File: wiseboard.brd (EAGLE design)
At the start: 100 x 80 mm, 87 parts, among them CN1 455-1749-1-ND, CN3 455-1749-1-ND, IC1 MCP73871-2CCI/ML-ND, IC2 LM358MX, Q1 IRLML6402TRPBF, Q2 IRLML6402TRPBF, U1 LT1945EMSPBF, X1 1528-1438-ND

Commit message: move all components onto test area and also test commit
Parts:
- moved R35 846.5 mm to (30.5, 38.1)
- moved R34 840.7 mm to (38.1, 38.1)
- moved R33 833.5 mm to (44.5, 36.8)
- moved S7 812.3 mm to (30.5, 34.3)
- moved S6 789.6 mm to (34.3, 30.5)
- moved S5 788.8 mm to (30.5, 50.8)
- moved S3 750.5 mm to (55.9, 45.7)
- moved S4 750.0 mm to (39.4, 29.2)
- moved C13 706.8 mm to (68.6, 7.62)
- moved C16 703.3 mm to (83.8, 78.7)
- moved JP3 703.3 mm to (78.7, 78.7)
- moved R20 703.3 mm to (80.0, 72.4)
- moved R29 703.3 mm to (80.0, 35.6)
- moved R30 703.3 mm to (80.0, 27.9)
- moved R31 703.3 mm to (80.0, 20.3)
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
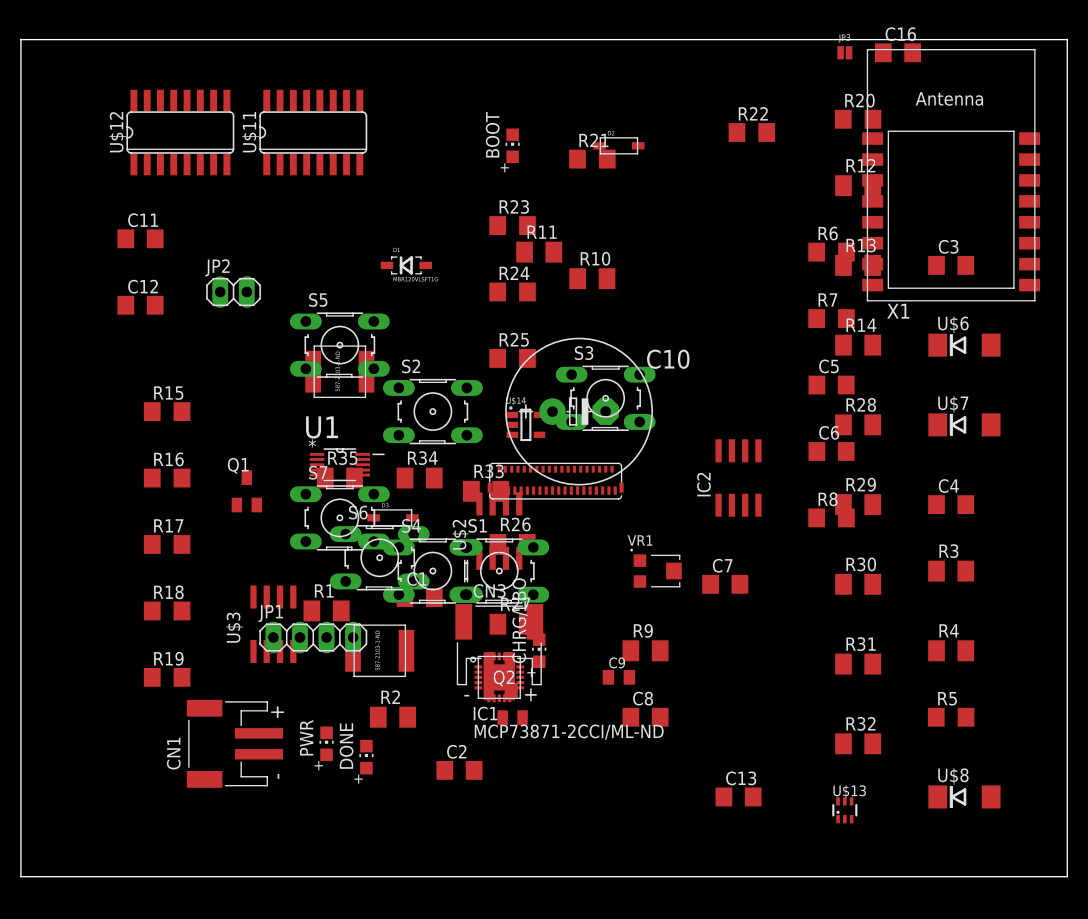
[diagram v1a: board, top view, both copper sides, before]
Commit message: ADD ESP DEBUG HEADERS AND ROUGH AUTOROUTE
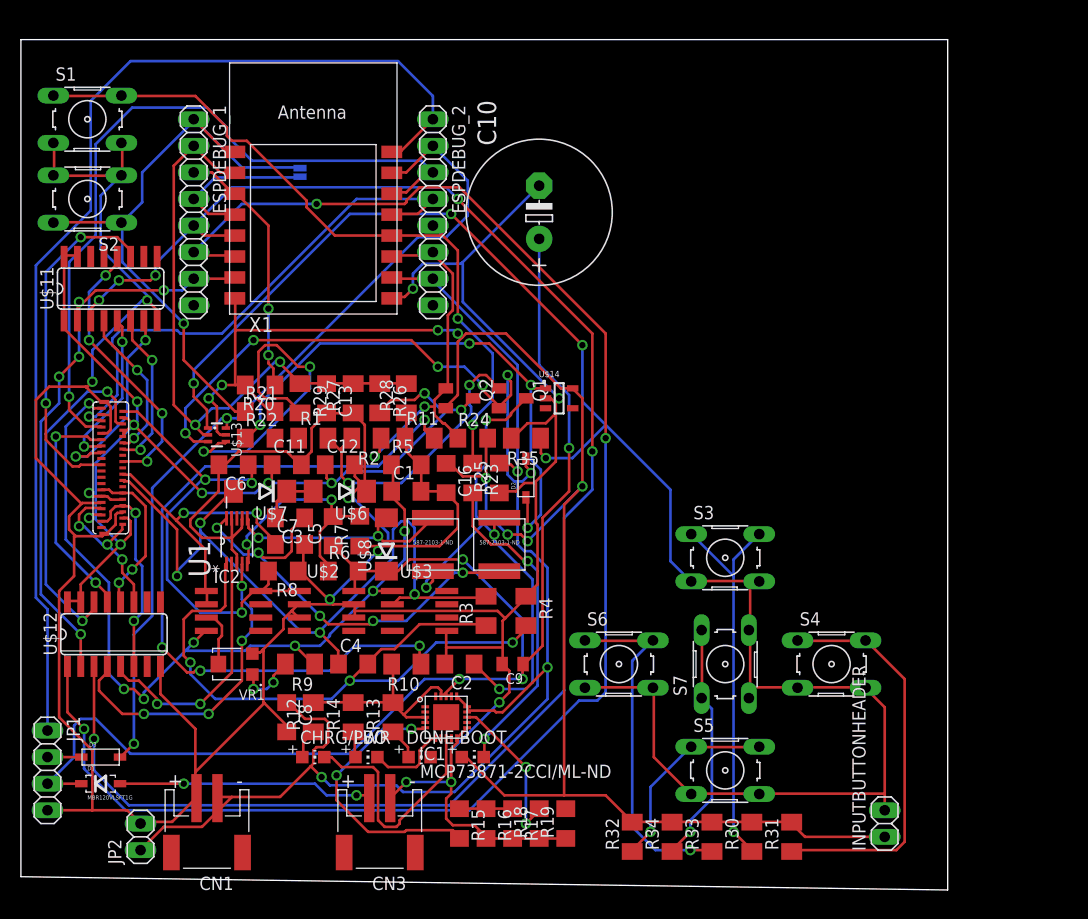
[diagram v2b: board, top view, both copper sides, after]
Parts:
- added ESPDEBUG_1, ESPDEBUG_2: (no value), pinhead:1X08
- added INPUTBUTTONHEADER: (no value), pinhead:1X02
- moved R12 72.7 mm to (27.9, 15.2), turned to 90 degrees
- moved U$13 69.9 mm to (18.7, 42.2), turned to 270 degrees
- moved C3 67.6 mm to (25.7, 34.3), turned to 180 degrees
- moved U$7 67.6 mm to (22.9, 36.8), turned to 180 degrees
- moved R20 62.5 mm to (22.9, 47.0), turned to 180 degrees
- moved R13 62.0 mm to (35.6, 15.2), turned to 90 degrees
- moved U$6 61.3 mm to (30.5, 36.8), turned to 180 degrees
- moved X1 61.0 mm to (27.9, 64.8)
- moved U$8 60.3 mm to (34.9, 31.8), turned to 90 degrees
- moved R14 59.9 mm to (31.8, 15.2), turned to 90 degrees
- moved C16 59.3 mm to (40.6, 38.1), turned to 270 degrees
- moved C4 59.1 mm to (31.8, 20.3)
- moved BOOT 58.5 mm to (43.2, 11.4), turned to 270 degrees
- moved S1 58.4 mm to (6.35, 72.4)
- moved D1 57.5 mm to (7.62, 8.89)
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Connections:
- removed net GPIO2: R24.1
- removed net N$12: JP3.1, X1.4
- removed net N$17: C8.1, CN1.2, IC1.14, IC1.15, IC1.16, JP2.1
- new net +3V1: ESPDEBUG_1.8
- new net GND1: ESPDEBUG_2.8
- new net GPIO16: ESPDEBUG_1.4, JP3.1, X1.4
- net +3V3: now also INPUTBUTTONHEADER.1
- net ADC: now also ESPDEBUG_1.2
- net BOOSTENA: now also ESPDEBUG_2.6, R24.1
- net CH_PD: now also ESPDEBUG_1.3
- net CL: now also ESPDEBUG_2.4
- net GPIO0: now also ESPDEBUG_2.5
- net GPIO12: now also ESPDEBUG_1.6; no longer U$13.6
- net GPIO13: now also ESPDEBUG_1.7
- net GPIO14: now also ESPDEBUG_1.5
- net GPIO15: now also ESPDEBUG_2.7
- net N$25: now also U$14.1
- net N$26: now also INPUTBUTTONHEADER.2
- net OE: now also ESPDEBUG_2.3
- net RESET: now also ESPDEBUG_1.1
- net RXD: now also ESPDEBUG_2.2, U$13.6
- net TXD: now also ESPDEBUG_2.1
- net VBAT: now also C8.1, CN1.2, IC1.14, IC1.15, IC1.16, JP2.1; no longer U$14.1
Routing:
- net GND: track 0.00 -> 404.0 mm, vias 0 -> 10
- net +3V3: track 0.00 -> 171.1 mm, vias 0 -> 8
- net N$26: track 0.00 -> 170.7 mm, vias 0 -> 4
- net GPIO14: track 0.00 -> 160.7 mm, vias 0 -> 6
- net VCC: track 0.00 -> 157.2 mm, vias 0 -> 4
- net GPIO12: track 0.00 -> 152.8 mm, vias 0 -> 3
- net VBAT: track 0.00 -> 150.4 mm, vias 0 -> 8
- net VDD: track 0.00 -> 106.8 mm, vias 0 -> 10
- net TXD: track 0.00 -> 105.9 mm
- net -15V: track 0.00 -> 82.1 mm, vias 0 -> 7
- net RXD: track 0.00 -> 82.0 mm, vias 0 -> 2
- net +20V: track 0.00 -> 72.7 mm, vias 0 -> 4
- net N$9: track 0.00 -> 72.5 mm, vias 0 -> 4
- net OE: track 0.00 -> 71.7 mm, vias 0 -> 1
- net GPIO0: track 0.00 -> 69.4 mm, vias 0 -> 2
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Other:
- board size 100 x 80 mm -> 88.6 x 81.3 mm

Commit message: PASS ERC SCHEMATIC TEST AND ADD SUPPLY SYMBOLS
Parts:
- removed C13: 1uF, adafruit:C1206
- added INPUTBUTTONHEADER1, SOLARPIN: (no value), pinhead:1X02
- C2: value (none) -> 2u2F
- C4: value (none) -> 100pF
- moved JP1 59.1 mm to (46.4, 49.8), turned to 180 degrees
- moved C10 53.1 mm to (26.7, 15.6), turned to 0 degrees
- moved IC2 52.9 mm to (-10.2, -17.8), turned to 0 degrees
- moved D3 52.7 mm to (47.6, 45.7), turned to 270 degrees
- moved ESPDEBUG_1 49.7 mm to (64.1, 49.2), turned to 180 degrees
- moved JP3 47.3 mm to (67.9, 44.1), turned to 0 degrees
- moved X1 46.5 mm to (66.7, 39.1), turned to 270 degrees
- moved BOOT 44.6 mm to (24.8, 52.1), turned to 180 degrees
- moved 22 44.0 mm to (3.81, 45.1)
- moved ESPDEBUG_2 43.1 mm to (64.1, 28.3), turned to 180 degrees
- moved C2 42.7 mm to (11.4, 50.2), turned to 0 degrees
- moved R4 42.5 mm to (14.6, 51.4), turned to 90 degrees
- moved R29 35.2 mm to (46.4, 16.5), turned to 0 degrees
- moved DONE 35.1 mm to (3.17, 7.62), turned to 90 degrees
- moved S2 34.6 mm to (37.5, 49.5), turned to 90 degrees
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- renumbered CN3 to SOLAR
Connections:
- net +20V renamed -20V
- removed net +24V: U$4.P$23
- removed net +3V1: ESPDEBUG_1.8
- removed net GND1: ESPDEBUG_2.8
- new net +22V: C5.1, R6.2, U$2.8, U$4.P$23, U$8.C
- net +3V3: now also ESPDEBUG_1.8, INPUTBUTTONHEADER1.1
- net ADC: no longer C13.1, U$13.2
- net GND: now also ESPDEBUG_2.8, SOLARPIN.1, U$13.2; no longer C13.2
- net GPIO16: now also JP3.2; no longer JP3.1
- net N$26: now also INPUTBUTTONHEADER1.2
- net N$7: now also SOLARPIN.2
- net RESET: now also JP3.1; no longer JP3.2
- net VCC: no longer C5.1, R6.2, U$2.8, U$8.C
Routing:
- net GND: track 404.0 -> 0.00 mm, vias 10 -> 0
- net +3V3: track 171.1 -> 0.00 mm, vias 8 -> 0
- net N$26: track 170.7 -> 0.00 mm, vias 4 -> 0
- net GPIO14: track 160.7 -> 0.00 mm, vias 6 -> 0
- net VCC: track 157.2 -> 0.00 mm, vias 4 -> 0
- net GPIO12: track 152.8 -> 0.00 mm, vias 3 -> 0
- net VBAT: track 150.4 -> 0.00 mm, vias 8 -> 0
- net VDD: track 106.8 -> 0.00 mm, vias 10 -> 0
- net TXD: track 105.9 -> 0.00 mm
- net -15V: track 82.1 -> 0.00 mm, vias 7 -> 0
- net RXD: track 82.0 -> 0.00 mm, vias 2 -> 0
- net -20V: track 72.7 -> 0.00 mm, vias 4 -> 0
- net N$9: track 72.5 -> 0.00 mm, vias 4 -> 0
- net OE: track 71.7 -> 0.00 mm, vias 1 -> 0
- net GPIO0: track 69.4 -> 0.00 mm, vias 2 -> 0
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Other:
- board size 88.6 x 81.3 mm -> 80 x 55 mm

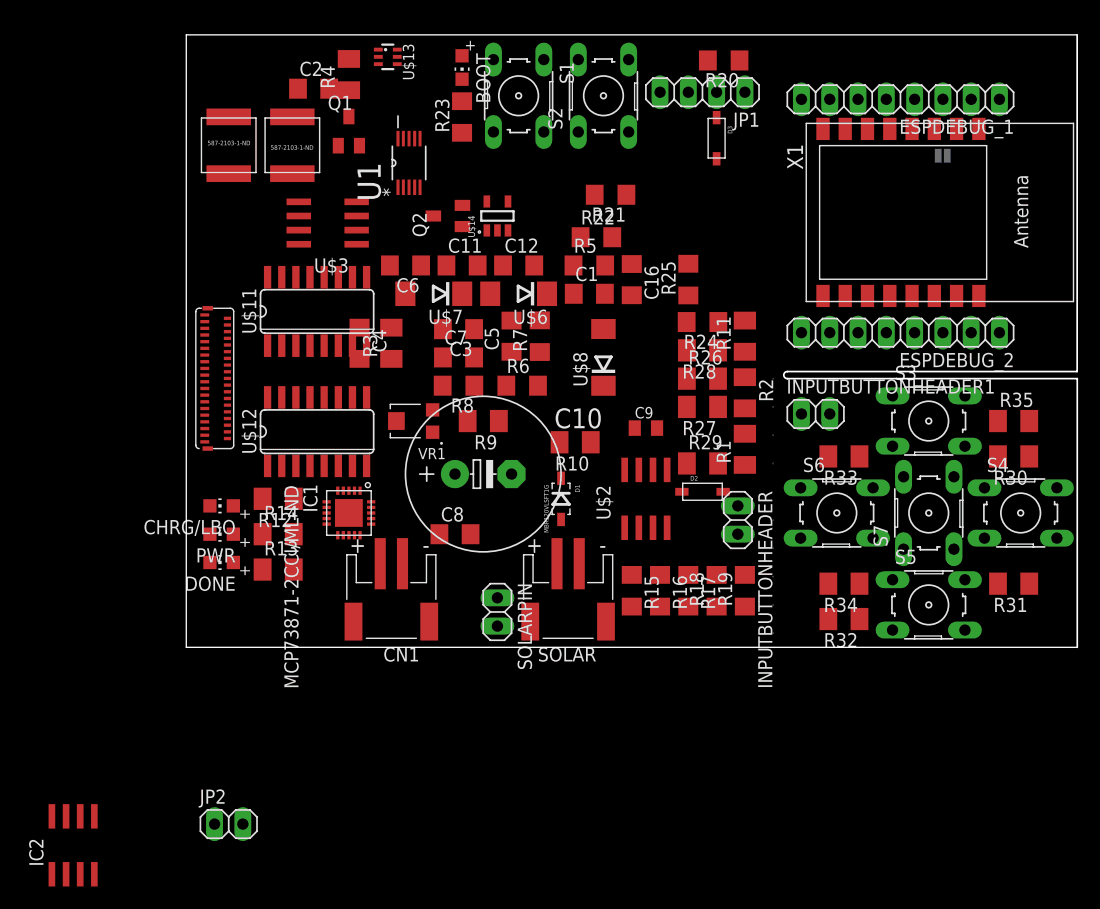
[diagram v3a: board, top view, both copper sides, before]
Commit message: ALMOST COMPLETE ROUTE OF MK1 PCB
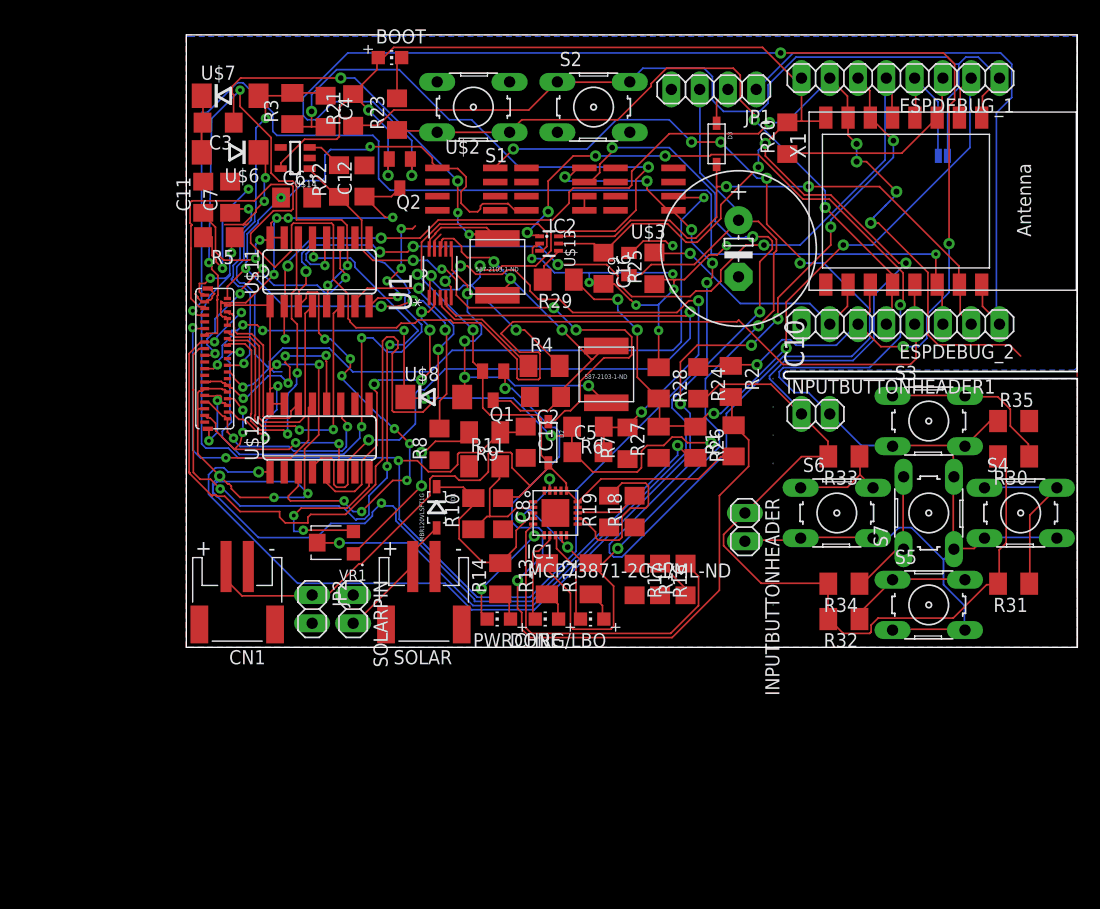
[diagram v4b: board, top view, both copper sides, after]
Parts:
- CN1: value 455-1749-1-ND -> (none)
- moved IC2 73.1 mm to (33.1, 41.1), turned to 90 degrees
- moved U$5 34.9 mm to (37.7, 24.5)
- moved CHRG/LBO 34.8 mm to (36.4, 2.54)
- moved C2 34.6 mm to (32.3, 22.5), turned to 180 degrees
- moved R5 33.4 mm to (2.92, 36.8), turned to 180 degrees
- moved U$2 32.2 mm to (25.1, 41.1), turned to 270 degrees
- moved R4 31.5 mm to (32.1, 25.3), turned to 0 degrees
- moved C10 30.6 mm to (49.6, 35.8), turned to 270 degrees
- moved DONE 29.6 mm to (32.4, 2.54)
- moved R12 29.0 mm to (36.3, 6.16), turned to 90 degrees
- moved U$6 28.9 mm to (3.94, 44.5)
- moved U$3 28.6 mm to (41.1, 41.1)
- moved C3 28.5 mm to (2.86, 47.1)
- moved 22 26.5 mm to (27.9, 34.2), turned to 90 degrees
- moved Q1 26.3 mm to (27.6, 23.5), turned to 180 degrees
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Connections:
- net GND: now also CN1.2; no longer CN1.1
- net VBAT: now also CN1.1; no longer CN1.2
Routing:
- net +3V3: track 0.00 -> 216.4 mm, vias 0 -> 5
- net VDD: track 0.00 -> 178.3 mm, vias 0 -> 15
- net +22V: track 0.00 -> 157.1 mm, vias 0 -> 12
- net N$26: track 0.00 -> 140.4 mm, vias 0 -> 5
- net -15V: track 0.00 -> 132.9 mm, vias 0 -> 8
- net BOOSTENA: track 0.00 -> 132.2 mm, vias 0 -> 5
- net CL: track 0.00 -> 122.3 mm
- net VCC: track 0.00 -> 119.5 mm, vias 0 -> 5
- net GND: track 0.00 -> 118.1 mm, vias 0 -> 20
- net GPIO14: track 0.00 -> 116.6 mm, vias 0 -> 13
- net GPIO12: track 0.00 -> 107.2 mm, vias 0 -> 6
- net VBAT: track 0.00 -> 106.8 mm, vias 0 -> 2
- net OE: track 0.00 -> 105.4 mm, vias 0 -> 2
- net GPIO13: track 0.00 -> 103.4 mm, vias 0 -> 8
- net -20V: track 0.00 -> 96.5 mm, vias 0 -> 3
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- added copper zone on layer 1, net GND
- added copper zone on layer 16, net N$12
